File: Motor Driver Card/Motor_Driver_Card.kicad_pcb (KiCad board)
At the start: 2 copper layers, 129.5 x 76.8 mm, 45 parts, among them J2 JST, J3 JST, J4 JST, J5 JST, M1 MD13B, M2 MD13B, M3 MD13B, M4 MD13B, Q1 2N3904, Q2 2N3904, Q3 2N3904, Q4 2N3904

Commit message: Complete redesign of PDB pcb
AAAAAAAAAAAAAAAAAAAAAAAAAAAAAAAAAAAAAAAAAAAA
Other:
- board text added: "ERRATA: BRIDGE GROUNDS BETWEEN MOTOR DRIVERS AND BACKPLANE"
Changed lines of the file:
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@@
+		)
+	)
+	(gr_text "ERRATA: BRIDGE GROUNDS BETWEEN MOTOR DRIVERS AND BACKPLANE"
+		(at 121.92 149.86 0)
+		(layer "User.1")
+		(effects
+			(font
+				(size 1.5 1.5)
+				(thickness 0.3)
+				(bold yes)
+			)
+			(justify left bottom)
 		)
 	)

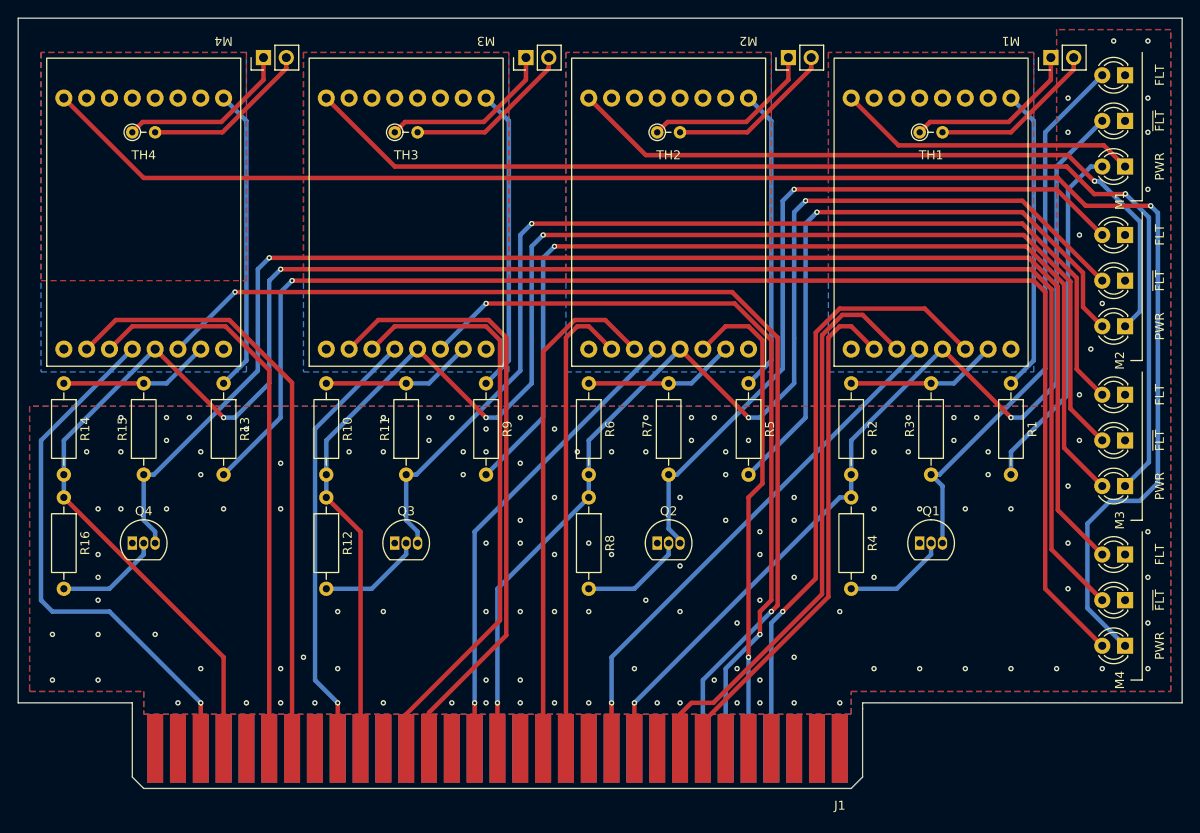
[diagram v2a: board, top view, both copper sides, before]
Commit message: Updated PCB designs across the motor driver, analog board, and PDB
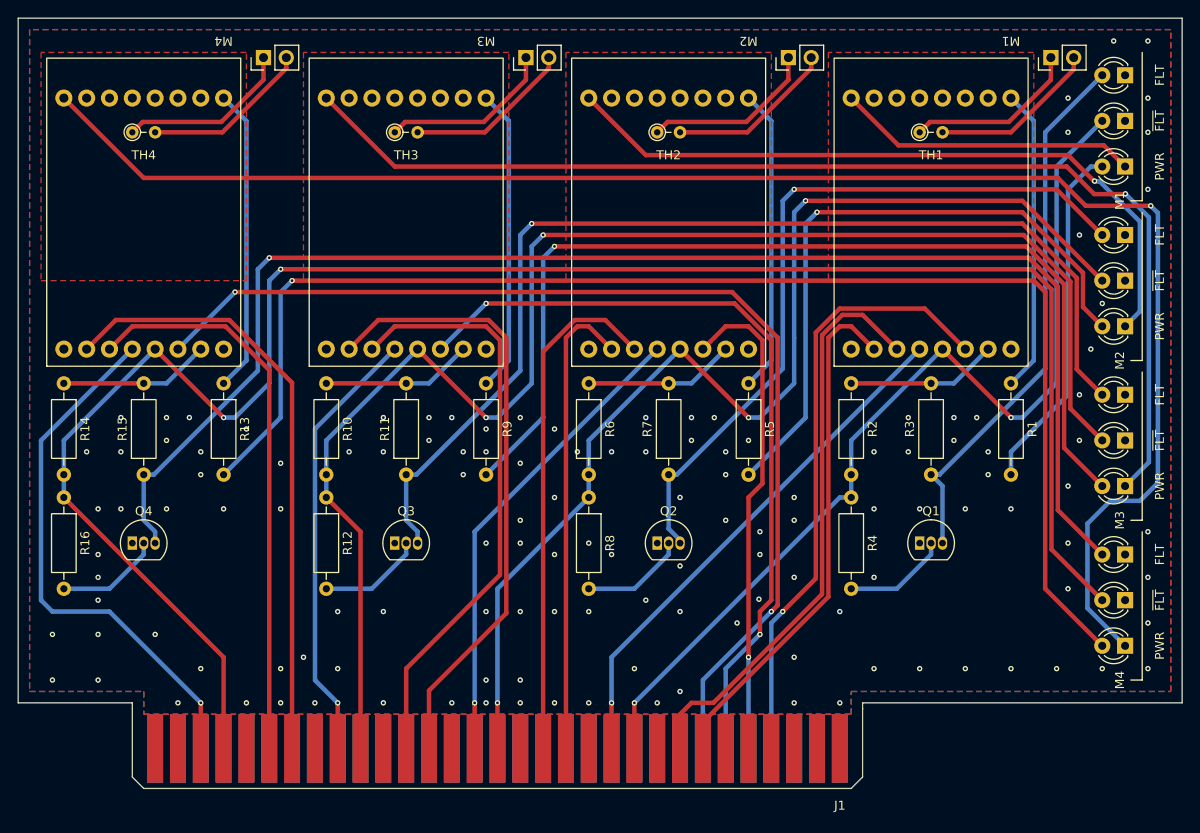
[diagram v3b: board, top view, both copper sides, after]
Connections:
- D1 pad 1: Net-(D1-K) -> GND
- D10 pad 1: Net-(D10-K) -> GND
- D4 pad 1: Net-(D4-K) -> GND
- D7 pad 1: Net-(D7-K) -> GND
- M1 pad 2: Net-(D1-K) -> GND
- M2 pad 2: Net-(D4-K) -> GND
- M3 pad 2: Net-(D7-K) -> GND
- M4 pad 2: Net-(D10-K) -> GND
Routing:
- net GND: track 0.00 -> 423.2 mm, vias 137 -> 135
- net Net-(D10-K): track 182.2 -> 0.00 mm, vias 1 -> 0
- net Net-(D7-K): track 128.1 -> 0.00 mm, vias 1 -> 0
- net Net-(D4-K): track 79.4 -> 0.00 mm, vias 1 -> 0
- net Net-(D1-K): track 33.6 -> 0.00 mm
- removed copper zone on B.Cu, net Net-(D1-K)
- removed copper zone on B.Cu, net Net-(D10-K)
- removed copper zone on B.Cu, net Net-(D4-K)
- removed copper zone on B.Cu, net Net-(D7-K)
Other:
- board text removed: "ERRATA: BRIDGE GROUNDS BETWEEN MOTOR DRIVERS AND BACKPLANE"
